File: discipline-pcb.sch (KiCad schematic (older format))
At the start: 165 parts, among them J1 AVR-ISP-6, SW1 KEYSW, SW10 KEYSW, SW11 KEYSW, SW12 KEYSW, SW13 KEYSW, SW14 KEYSW, SW15 Rotary_Encoder_Switch, SW16 KEYSW, SW17 KEYSW, SW18 KEYSW, SW19 KEYSW, SW2 KEYSW, SW20 KEYSW, SW21 KEYSW, SW22 KEYSW, SW23 KEYSW, SW24 KEYSW, SW25 KEYSW, SW26 KEYSW, SW27 KEYSW, SW28 KEYSW, SW29 KEYSW, SW3 KEYSW, SW30 KEYSW, SW31 KEYSW, SW32 KEYSW, SW33 KEYSW, SW34 KEYSW, SW35 KEYSW, SW36 KEYSW, SW37 KEYSW, SW38 KEYSW, SW39 KEYSW, SW4 KEYSW, SW40 KEYSW, SW41 KEYSW, SW42 KEYSW, SW43 KEYSW, SW44 KEYSW, SW45 KEYSW, SW46 KEYSW, SW47 KEYSW, SW48 KEYSW, SW49 KEYSW, SW5 KEYSW, SW50 KEYSW, SW51 KEYSW, SW52 KEYSW, SW53 KEYSW, SW54 KEYSW, SW55 KEYSW, SW56 KEYSW, SW57 KEYSW, SW58 KEYSW, SW59 KEYSW, SW6 KEYSW, SW60 KEYSW, SW61 KEYSW, SW62 KEYSW, SW63 KEYSW, SW64 KEYSW, SW65 KEYSW, SW66 KEYSW, SW67 KEYSW, SW68 KEYSW, SW69 KEYSW, SW7 KEYSW, SW70 KEYSW, SW71 KEYSW, SW72 KEYSW, SW73 KEYSW, SW74 KEYSW, SW8 KEYSW, SW9 KEYSW, U1 ATmega32A-PU, Y1 Crystal

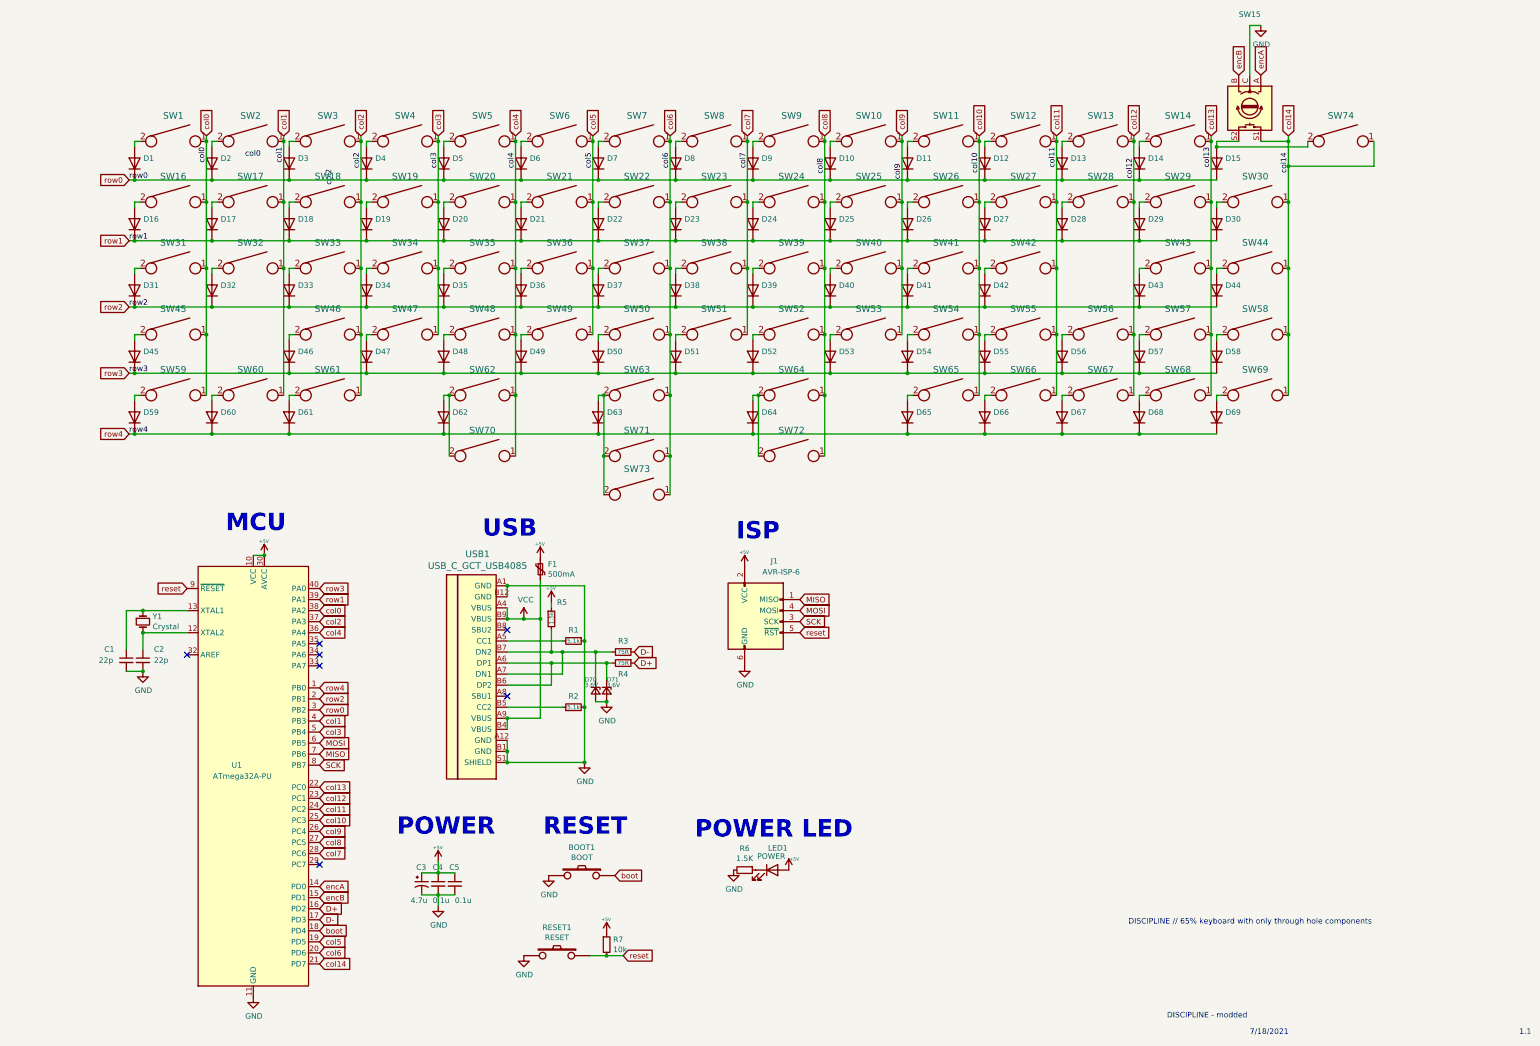
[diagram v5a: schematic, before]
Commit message: added 3x1u and 2x1.5u options in bottom right modifier section. renumbered switches and diodes
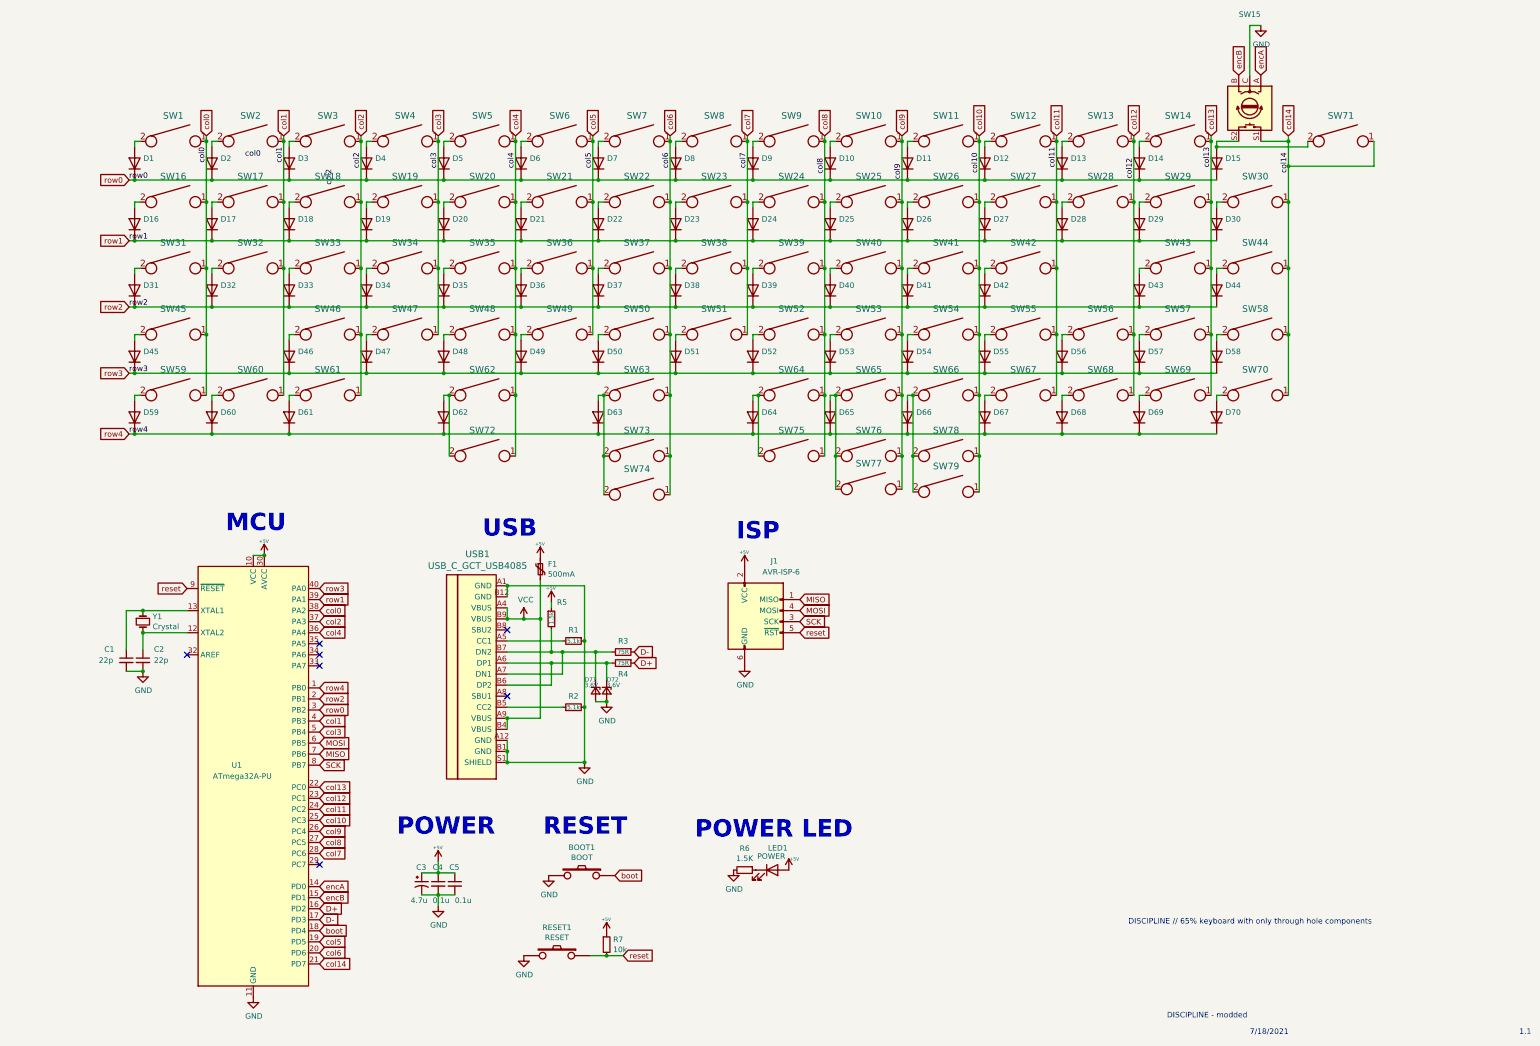
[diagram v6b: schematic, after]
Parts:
- added D65: (no value), cftkb:D_DO-35_SOD27_P5.08mm_Horizontal, symbol Device:D
- added SW65: KEYSW-keyboard_parts, cftkb:SW_Cherry_MX1A_1.00u_PCB-NOSCREEN, symbol discipline-pcb-rescue:KEYSW-keyboard_parts
- added SW76, SW78: KEYSW-keyboard_parts, cftkb:SW_Cherry_MX1A_1.25u_PCBNOSCREEN, symbol discipline-pcb-rescue:KEYSW-keyboard_parts
- added SW77, SW79: KEYSW-keyboard_parts, cftkb:SW_Cherry_MX1A_1.50u_PCBNOSCREEN, symbol discipline-pcb-rescue:KEYSW-keyboard_parts
- SW66: renamed from SW65; footprint cftkb:SW_Cherry_MX1A_1.25u_PCBNOSCREEN -> cftkb:SW_Cherry_MX1A_1.00u_PCB-NOSCREEN
- SW67: renamed from SW66; footprint cftkb:SW_Cherry_MX1A_1.25u_PCBNOSCREEN -> cftkb:SW_Cherry_MX1A_1.00u_PCB-NOSCREEN
- renumbered D65 to D66, D66 to D67, D67 to D68, D68 to D69, D69 to D70, D70 to D71, D71 to D72, SW67 to SW68, SW68 to SW69, SW69 to SW70, SW74 to SW71, SW70 to SW72, SW71 to SW73, SW73 to SW74, SW72 to SW75
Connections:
- net col10: now also SW78.1, SW79.1
- net col9: now also SW65.1, SW76.1, SW77.1
- net row4: now also D65.1 (K)
- net at D66.2 (A), SW66.2: now also SW78.2, SW79.2
- new net: D65.2 (A), SW65.2, SW76.2, SW77.2
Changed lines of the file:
@@
 	7100 5250 7100 5300
 $Comp
-L discipline-pcb-rescue:KEYSW-keyboard_parts SW66
+L discipline-pcb-rescue:KEYSW-keyboard_parts SW67
 U 1 1 5BE881B1
 P 10950 5250
-F 0 "SW66" H 10950 5483 60  0000 C CNN
+F 0 "SW67" H 10950 5483 60  0000 C CNN
 F 1 "KEYSW" H 10950 5150 60  0001 C CNN
-F 2 "cftkb:SW_Cherry_MX1A_1.25u_PCBNOSCREEN" H 10950 5250 60  0001 C CNN
+F 2 "cftkb:SW_Cherry_MX1A_1.00u_PCB-NOSCREEN" H 10950 5250 60  0001 C CNN
 F 3 "" H 10950 5250 60  0000 C CNN
 	1    10950 5250
@@
 $EndComp
 $Comp
-L Device:D D66
+L Device:D D67
 U 1 1 5BE881B8
 P 10600 5450
-F 0 "D66" V 10646 5371 50  0000 R CNN
+F 0 "D67" V 10646 5371 50  0000 R CNN
 F 1 " " V 10555 5371 50  0000 R CNN
 F 2 "cftkb:D_DO-35_SOD27_P5.08mm_Horizontal" H 10600 5450 50  0001 C CNN
@@
 	10600 5250 10600 5300
 $Comp
-L discipline-pcb-rescue:KEYSW-keyboard_parts SW65
+L discipline-pcb-rescue:KEYSW-keyboard_parts SW66
 U 1 1 5BE881C1
 P 10250 5250
-F 0 "SW65" H 10250 5483 60  0000 C CNN
+F 0 "SW66" H 10250 5483 60  0000 C CNN
 F 1 "KEYSW" H 10250 5150 60  0001 C CNN
-F 2 "cftkb:SW_Cherry_MX1A_1.25u_PCBNOSCREEN" H 10250 5250 60  0001 C CNN
+F 2 "cftkb:SW_Cherry_MX1A_1.00u_PCB-NOSCREEN" H 10250 5250 60  0001 C CNN
 F 3 "" H 10250 5250 60  0000 C CNN
 	1    10250 5250
@@
 $EndComp
 $Comp
-L Device:D D65
+L Device:D D66
 U 1 1 5BE881C8
 P 9900 5450
-F 0 "D65" V 9946 5371 50  0000 R CNN
+F 0 "D66" V 9946 5371 50  0000 R CNN
 F 1 " " V 9855 5371 50  0000 R CNN
 F 2 "cftkb:D_DO-35_SOD27_P5.08mm_Horizontal" H 9900 5450 50  0001 C CNN
@@
 	9900 5250 9900 5300
 $Comp
-L discipline-pcb-rescue:KEYSW-keyboard_parts SW67
+L discipline-pcb-rescue:KEYSW-keyboard_parts SW68
 U 1 1 5BE881D1
 P 11650 5250
-F 0 "SW67" H 11650 5483 60  0000 C CNN
+F 0 "SW68" H 11650 5483 60  0000 C CNN
 F 1 "KEYSW" H 11650 5150 60  0001 C CNN
 F 2 "cftkb:SW_Cherry_MX1A_1.00u_PCB-NOSCREEN" H 11650 5250 60  0001 C CNN
@@
 $EndComp
 $Comp
-L Device:D D67
+L Device:D D68
 U 1 1 5BE881D8
 P 11300 5450
-F 0 "D67" V 11346 5371 50  0000 R CNN
+F 0 "D68" V 11346 5371 50  0000 R CNN
 F 1 " " V 11255 5371 50  0000 R CNN
 F 2 "cftkb:D_DO-35_SOD27_P5.08mm_Horizontal" H 11300 5450 50  0001 C CNN
@@
 	11300 5250 11300 5300
 $Comp
-L discipline-pcb-rescue:KEYSW-keyboard_parts SW68
+L discipline-pcb-rescue:KEYSW-keyboard_parts SW69
 U 1 1 5BE881E1
 P 12350 5250
-F 0 "SW68" H 12350 5483 60  0000 C CNN
+F 0 "SW69" H 12350 5483 60  0000 C CNN
 F 1 "KEYSW" H 12350 5150 60  0001 C CNN
 F 2 "cftkb:SW_Cherry_MX1A_1.00u_PCB-NOSCREEN" H 12350 5250 60  0001 C CNN
@@
 $EndComp
 $Comp
-L Device:D D68
+L Device:D D69
 U 1 1 5BE881E8
 P 12000 5450
-F 0 "D68" V 12046 5371 50  0000 R CNN
+F 0 "D69" V 12046 5371 50  0000 R CNN
 F 1 " " V 11955 5371 50  0000 R CNN
 F 2 "cftkb:D_DO-35_SOD27_P5.08mm_Horizontal" H 12000 5450 50  0001 C CNN
@@
 	12000 5250 12000 5300
 $Comp
-L discipline-pcb-rescue:KEYSW-keyboard_parts SW69
+L discipline-pcb-rescue:KEYSW-keyboard_parts SW70
 U 1 1 5BE881F1
 P 13050 5250
-F 0 "SW69" H 13050 5483 60  0000 C CNN
+F 0 "SW70" H 13050 5483 60  0000 C CNN
 F 1 "KEYSW" H 13050 5150 60  0001 C CNN
 F 2 "cftkb:SW_Cherry_MX1A_1.00u_PCB-NOSCREEN" H 13050 5250 60  0001 C CNN
@@
 $EndComp
 $Comp
-L Device:D D69
+L Device:D D70
 U 1 1 5BE881F8
 P 12700 5450
-F 0 "D69" V 12746 5371 50  0000 R CNN
+F 0 "D70" V 12746 5371 50  0000 R CNN
 F 1 " " V 12655 5371 50  0000 R CNN
 F 2 "cftkb:D_DO-35_SOD27_P5.08mm_Horizontal" H 12700 5450 50  0001 C CNN
@@
 Connection ~ 2975 7750
 $Comp
-L Device:D_Zener_Small D70
+L Device:D_Zener_Small D71
 U 1 1 5D184B7B
 P 7075 7925
-F 0 "D70" V 6975 7825 39  0000 L CNN
+F 0 "D71" V 6975 7825 39  0000 L CNN
 F 1 "3.6V" V 7025 8025 39  0000 L CNN
 F 2 "cftkb:D_DO-35_SOD27_P5.08mm_Horizontal" V 7075 7925 50  0001 C CNN
@@
 $EndComp
 $Comp
-L Device:D_Zener_Small D71
+L Device:D_Zener_Small D72
 U 1 1 5D184D75
 P 7175 7925
-F 0 "D71" V 7075 7925 39  0000 L CNN
+F 0 "D72" V 7075 7925 39  0000 L CNN
 F 1 "3.6V" V 7125 7725 39  0000 L CNN
 F 2 "cftkb:D_DO-35_SOD27_P5.08mm_Horizontal" V 7175 7925 50  0001 C CNN
@@
 Connection ~ 10550 4700
 Wire Wire Line
-	10550 4700 10550 5250
-Wire Wire Line
 	11250 2900 11250 2950
 Connection ~ 11250 2950
@@
 Wire Wire Line
 	12650 4100 12650 4700
-Wire Wire Line
-	9900 5600 10600 5600
 $Comp
 L discipline-pcb-rescue:KEYSW-keyboard_parts SW62
@@
 	1    0    0    -1
 $EndComp
-Connection ~ 10600 5600
-Wire Wire Line
-	10600 5600 11300 5600
 Wire Wire Line
 	7100 5600 8500 5600
@@
 Connection ~ 8500 5600
 Wire Wire Line
-	8500 5600 9900 5600
+	8500 5600 9200 5600
 Wire Wire Line
 	5750 5250 5700 5250
@@
 $EndComp
 $Comp
-L discipline-pcb-rescue:KEYSW-keyboard_parts SW70
+L discipline-pcb-rescue:KEYSW-keyboard_parts SW72
 U 1 1 6169457F
 P 6050 5800
-F 0 "SW70" H 6050 6033 60  0000 C CNN
+F 0 "SW72" H 6050 6033 60  0000 C CNN
 F 1 "KEYSW" H 6050 5700 60  0001 C CNN
 F 2 "cftkb:SW_Cherry_MX_2.25u_PCB_nosilk_fliippedstabs" H 6050 5800 60  0001 C CNN
@@
 Connection ~ 9150 5250
 $Comp
-L discipline-pcb-rescue:KEYSW-keyboard_parts SW71
+L discipline-pcb-rescue:KEYSW-keyboard_parts SW73
 U 1 1 6173414E
 P 7450 5800
-F 0 "SW71" H 7450 6033 60  0000 C CNN
+F 0 "SW73" H 7450 6033 60  0000 C CNN
 F 1 "KEYSW" H 7450 5700 60  0001 C CNN
 F 2 "cftkb:SW_Cherry_MX1A_1.25u_PCBNOSCREEN" H 7450 5800 60  0001 C CNN
@@
 $EndComp
 $Comp
-L discipline-pcb-rescue:KEYSW-keyboard_parts SW72
+L discipline-pcb-rescue:KEYSW-keyboard_parts SW75
 U 1 1 61735BD7
 P 8850 5800
-F 0 "SW72" H 8850 6033 60  0000 C CNN
+F 0 "SW75" H 8850 6033 60  0000 C CNN
 F 1 "KEYSW" H 8850 5700 60  0001 C CNN
 F 2 "cftkb:SW_Cherry_MX_2.75u_PCB_nosilk_flippedstabs" H 8850 5800 60  0001 C CNN
@@
 Connection ~ 7750 5250
 $Comp
-L discipline-pcb-rescue:KEYSW-keyboard_parts SW73
+L discipline-pcb-rescue:KEYSW-keyboard_parts SW74
 U 1 1 6179ACA3
 P 7450 6150
-F 0 "SW73" H 7450 6383 60  0000 C CNN
+F 0 "SW74" H 7450 6383 60  0000 C CNN
 F 1 "KEYSW" H 7450 6050 60  0001 C CNN
 F 2 "cftkb:SW_Cherry_MX_6.25u_PCB_nosilk_flippedstabs" H 7450 6150 60  0001 C CNN
@@
 NoConn ~ 4575 7700
 $Comp
-L discipline-pcb-rescue:KEYSW-keyboard_parts SW74
+L discipline-pcb-rescue:KEYSW-keyboard_parts SW71
 U 1 1 60F8FE34
 P 13825 2950
-F 0 "SW74" H 13825 3183 60  0000 C CNN
+F 0 "SW71" H 13825 3183 60  0000 C CNN
 F 1 "KEYSW" H 13825 2850 60  0001 C CNN
 F 2 "cftkb:SW_Cherry_MX1A_1.00u_PCB-NOSCREEN" H 13825 2950 60  0001 C CNN
@@
 Wire Wire Line
 	13350 3175 13350 3500
+$Comp
+L discipline-pcb-rescue:KEYSW-keyboard_parts SW76
+U 1 1 6159E32C
+P 9550 5800
+F 0 "SW76" H 9550 6033 60  0000 C CNN
+F 1 "KEYSW-keyboard_parts" H 9550 5700 60  0001 C CNN
+F 2 "cftkb:SW_Cherry_MX1A_1.25u_PCBNOSCREEN" H 9550 5800 60  0001 C CNN
+F 3 "" H 9550 5800 60  0000 C CNN
+	1    9550 5800
+	1    0    0    -1
+$EndComp
+$Comp
+L discipline-pcb-rescue:KEYSW-keyboard_parts SW65
+U 1 1 615A03E9
+P 9550 5250
+F 0 "SW65" H 9550 5483 60  0000 C CNN
+F 1 "KEYSW-keyboard_parts" H 9550 5150 60  0001 C CNN
+F 2 "cftkb:SW_Cherry_MX1A_1.00u_PCB-NOSCREEN" H 9550 5250 60  0001 C CNN
+F 3 "" H 9550 5250 60  0000 C CNN
+	1    9550 5250
+	1    0    0    -1
+$EndComp
+$Comp
+L discipline-pcb-rescue:KEYSW-keyboard_parts SW78
+U 1 1 615A18FC
+P 10250 5800
+F 0 "SW78" H 10250 6033 60  0000 C CNN
+F 1 "KEYSW-keyboard_parts" H 10250 5700 60  0001 C CNN
+F 2 "cftkb:SW_Cherry_MX1A_1.25u_PCBNOSCREEN" H 10250 5800 60  0001 C CNN
+F 3 "" H 10250 5800 60  0000 C CNN
+	1    10250 5800
+	1    0    0    -1
+$EndComp
+$Comp
+L discipline-pcb-rescue:KEYSW-keyboard_parts SW77
+U 1 1 615A8BE1
+P 9550 6100
+F 0 "SW77" H 9550 6333 60  0000 C CNN
+F 1 "KEYSW-keyboard_parts" H 9550 6000 60  0001 C CNN
+F 2 "cftkb:SW_Cherry_MX1A_1.50u_PCBNOSCREEN" H 9550 6100 60  0001 C CNN
+F 3 "" H 9550 6100 60  0000 C CNN
+	1    9550 6100
+	1    0    0    -1
+$EndComp
+$Comp
+L discipline-pcb-rescue:KEYSW-keyboard_parts SW79
+U 1 1 615A8FDF
+P 10250 6125
+F 0 "SW79" H 10250 6358 60  0000 C CNN
+F 1 "KEYSW-keyboard_parts" H 10250 6025 60  0001 C CNN
+F 2 "cftkb:SW_Cherry_MX1A_1.50u_PCBNOSCREEN" H 10250 6125 60  0001 C CNN
+F 3 "" H 10250 6125 60  0000 C CNN
+	1    10250 6125
+	1    0    0    -1
+$EndComp
+Wire Wire Line
+	9900 5600 10600 5600
+Wire Wire Line
+	9950 5250 9950 5800
+Connection ~ 9950 5250
+Wire Wire Line
+	9950 6125 9950 5800
+Connection ~ 9950 5800
+Wire Wire Line
+	10550 5250 10550 5800
+Connection ~ 10550 5250
+Wire Wire Line
+	10550 5800 10550 6125
+Connection ~ 10550 5800
+$Comp
+L Device:D D65
+U 1 1 616E0C3C
+P 9200 5450
+F 0 "D65" V 9246 5371 50  0000 R CNN
+F 1 " " V 9155 5371 50  0000 R CNN
+F 2 "cftkb:D_DO-35_SOD27_P5.08mm_Horizontal" H 9200 5450 50  0001 C CNN
+F 3 "~" H 9200 5450 50  0001 C CNN
+	1    9200 5450
+	0    -1   -1   0
+$EndComp
+Connection ~ 10600 5600
+Connection ~ 9200 5600
+Wire Wire Line
+	9200 5300 9200 5250
+Wire Wire Line
+	9200 5250 9250 5250
+Wire Wire Line
+	9200 5600 9900 5600
+Wire Wire Line
+	10550 4700 10550 5250
+Wire Wire Line
+	10600 5600 11300 5600
+Wire Wire Line
+	9850 4700 9850 5250
+Connection ~ 9850 4700
+Wire Wire Line
+	9250 5250 9250 5800
+Wire Wire Line
+	9250 5800 9250 6100
+Connection ~ 9250 5250
+Connection ~ 9250 5800
+Wire Wire Line
+	9850 5250 9850 5800
+Connection ~ 9850 5250
+Wire Wire Line
+	9850 6100 9850 5800
+Connection ~ 9850 5800
 $EndSCHEMATC

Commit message: replaced reset and boot buttons with right angle buttons
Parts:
- BOOT1, RESET1: footprint cftkb:SW_PUSH_6mm -> Button_Switch_THT:SW_Tactile_SPST_Angled_PTS645Vx31-2LFS
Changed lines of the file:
@@
 F 0 "RESET1" H 6725 10580 50  0000 C CNN
 F 1 "RESET" H 6725 10489 50  0000 C CNN
-F 2 "cftkb:SW_PUSH_6mm" H 6725 10325 60  0001 C CNN
+F 2 "Button_Switch_THT:SW_Tactile_SPST_Angled_PTS645Vx31-2LFS" H 6725 10325 60  0001 C CNN
 F 3 "" H 6725 10325 60  0000 C CNN
 	1    6725 10325
@@
 F 0 "BOOT1" H 6950 9855 50  0000 C CNN
 F 1 "BOOT" H 6950 9764 50  0000 C CNN
-F 2 "cftkb:SW_PUSH_6mm" H 6950 9600 60  0001 C CNN
+F 2 "Button_Switch_THT:SW_Tactile_SPST_Angled_PTS645Vx31-2LFS" H 6950 9600 60  0001 C CNN
 F 3 "" H 6950 9600 60  0000 C CNN
 	1    6950 9600
